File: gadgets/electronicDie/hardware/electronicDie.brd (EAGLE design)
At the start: 43.2 x 69.8 mm, 32 parts, among them IC1 CD4029N, IC2 NE555N, T1 BC327, T2 BC337, X1 USBPCB

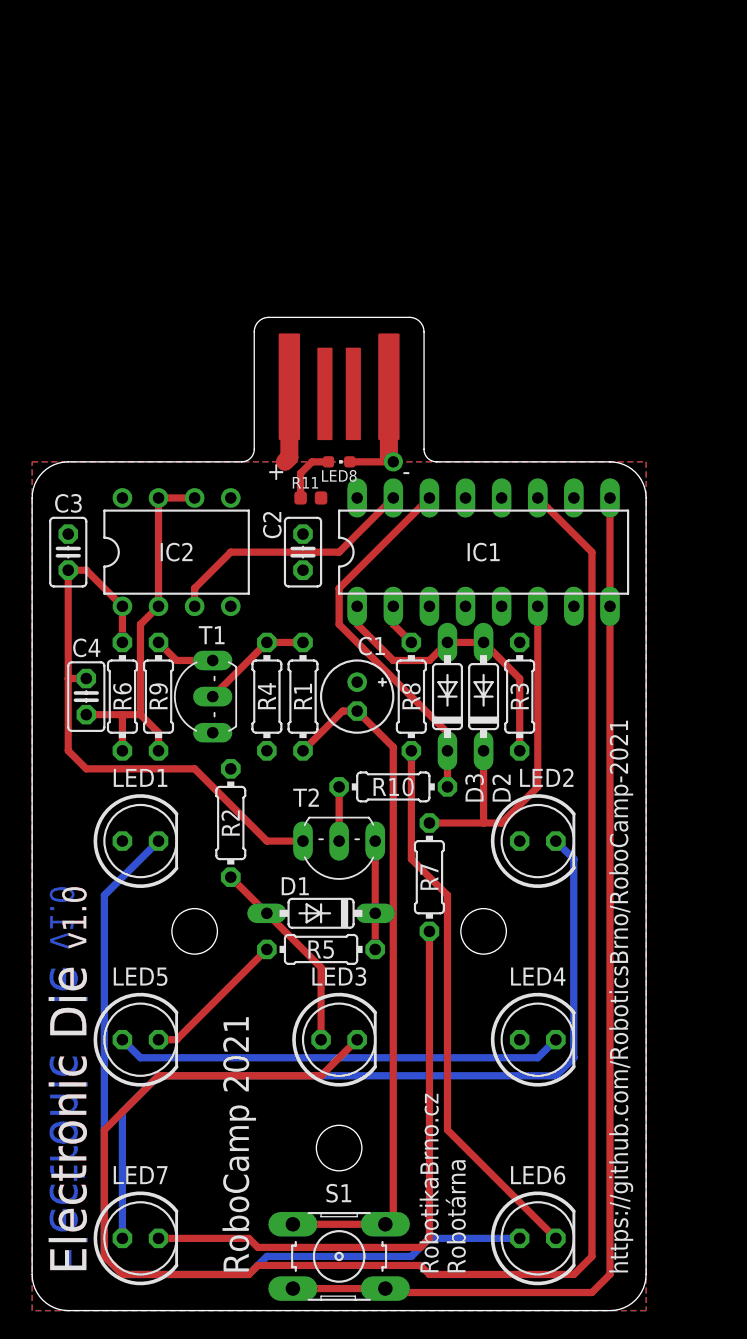
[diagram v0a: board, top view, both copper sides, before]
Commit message: ElectronicDie: fix v1.0 problems - make it bigger - change resistors and diodes package size - make larger spaces between parts - minimize part types - fix PNP transistor pinout - remove SMD power LED
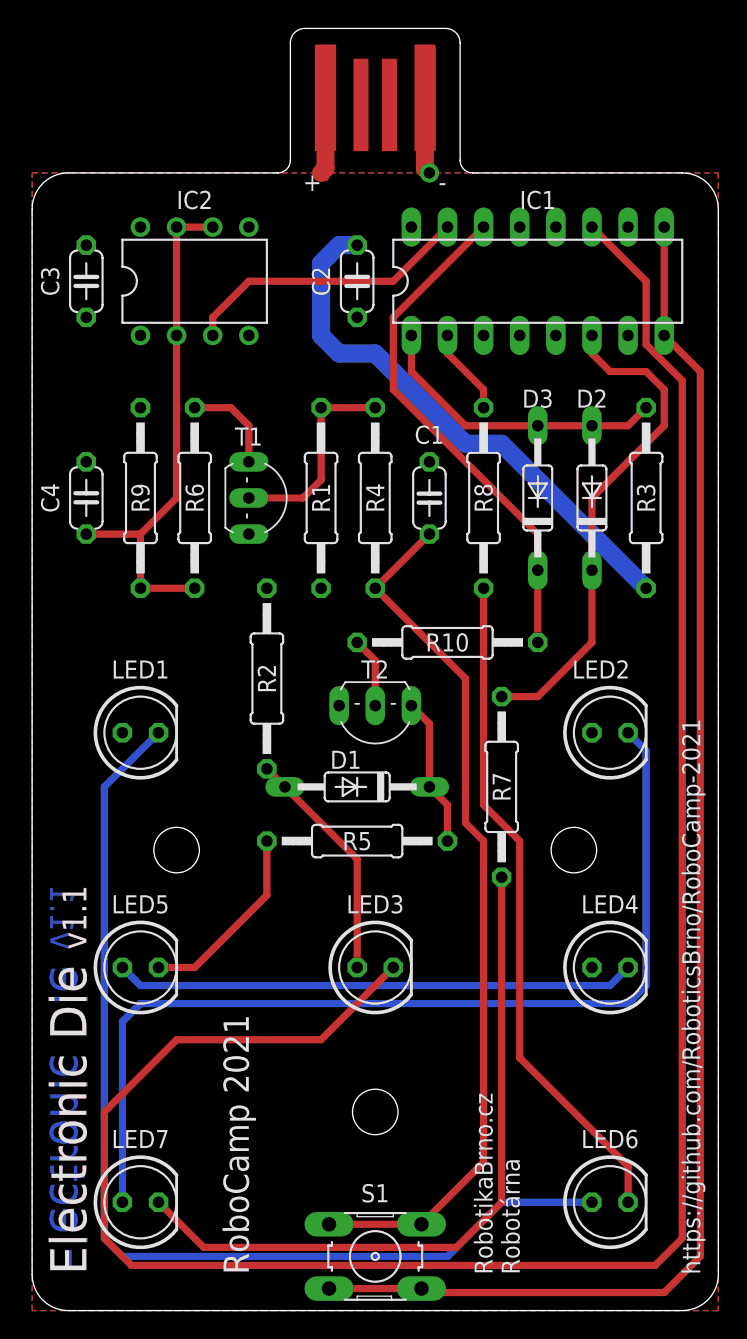
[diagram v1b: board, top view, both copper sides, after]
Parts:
- removed LED8: green, led:CHIPLED_0603
- removed R11: 1k, rcl_upravena:R0603
- C1: value 1u -> 100n; device rcl_upravena:E2-5 -> rcl_upravena:C050-024X044
- C2, C3, C4: device rcl_upravena:C025-025X050 -> rcl_upravena:C050-024X044
- D1, D2, D3: device diode:DO35-7 -> diode:DO35-10
- R1: value 3M3 -> 4M7; device rcl_upravena:0204/7 -> rcl_upravena:0207/12
- R10, R3: value 100k -> 10k; device rcl_upravena:0204/7 -> rcl_upravena:0207/12
- R2, R5, R6, R7, R8, R9: device rcl_upravena:0204/7 -> rcl_upravena:0207/12
- R4: value 10M -> 4M7; device rcl_upravena:0204/7 -> rcl_upravena:0207/12
- T1: value BC327 -> BC557B; device transistor:TO92-EBC -> transistor:TO92-CBE
- T2: value BC337 -> BC547B
- moved X1 20.5 mm to (24.1, 85.1)
- moved C2 19.4 mm to (22.9, 72.4)
- moved IC1 19.4 mm to (35.6, 72.4)
- moved C3 19.1 mm to (3.81, 72.4)
- moved IC2 19.1 mm to (11.4, 72.4)
- moved R3 16.6 mm to (43.2, 57.1), turned to 270 degrees
- moved D2 15.9 mm to (39.4, 57.1)
- moved D3 15.3 mm to (35.6, 57.1)
- moved C1 14.9 mm to (27.9, 57.1)
- moved R4 14.9 mm to (24.1, 57.1)
- moved R8 14.9 mm to (31.8, 57.1)
- moved R1 14.5 mm to (20.3, 57.1)
- moved T1 14.5 mm to (15.2, 57.1), turned to 270 degrees
- moved R6 14.2 mm to (11.4, 57.1)
- moved R9 14.0 mm to (7.62, 57.1)
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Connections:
- removed net N$3: LED8.A, R11.1
- net +5V: now also C1.1; no longer C1.+, R11.2
- net GND: no longer LED8.C
- net N$1: now also C1.2; no longer C1.-
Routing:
- net +5V: track 5.41 -> 44.4 mm
- net N$20: track 120.1 -> 149.4 mm
- net GND: track 126.5 -> 106.1 mm
- net N$1: track 48.8 -> 61.6 mm
- net N$16: track 61.6 -> 73.5 mm
- net N$14: track 58.0 -> 68.9 mm
- net N$11: track 26.1 -> 36.0 mm
- net N$5: track 27.7 -> 36.6 mm
- net N$22: track 38.5 -> 47.4 mm
- net N$10: track 26.5 -> 35.2 mm
- net N$8: track 41.2 -> 49.6 mm
- net N$2: track 7.93 -> 14.5 mm
- net N$13: track 31.5 -> 36.6 mm
- net N$3: track 4.03 -> 0.00 mm
- net N$18: track 10.3 -> 13.5 mm
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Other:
- board size 43.2 x 69.8 mm -> 48.3 x 90.2 mm
- board text added: "v1.1"
- board text removed: "v1.0"

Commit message: ElectronicDie v1.2: more resistant to assembly errors - resistors with same value grouped together - diodes grouped together - larger spaces between parts - 2k2 resistor replaced with 2 × 1k (so only 3 types of resistors left: 1k, 10k and 4M7) - added parts value to silkscreen - URL in silkscreen changed from robotikabrno.cz to robotickytabor.cz - changed year of Robocamp to 2022 (but 2021 remains in repo URL) - added silkscreen label for engraving owner name
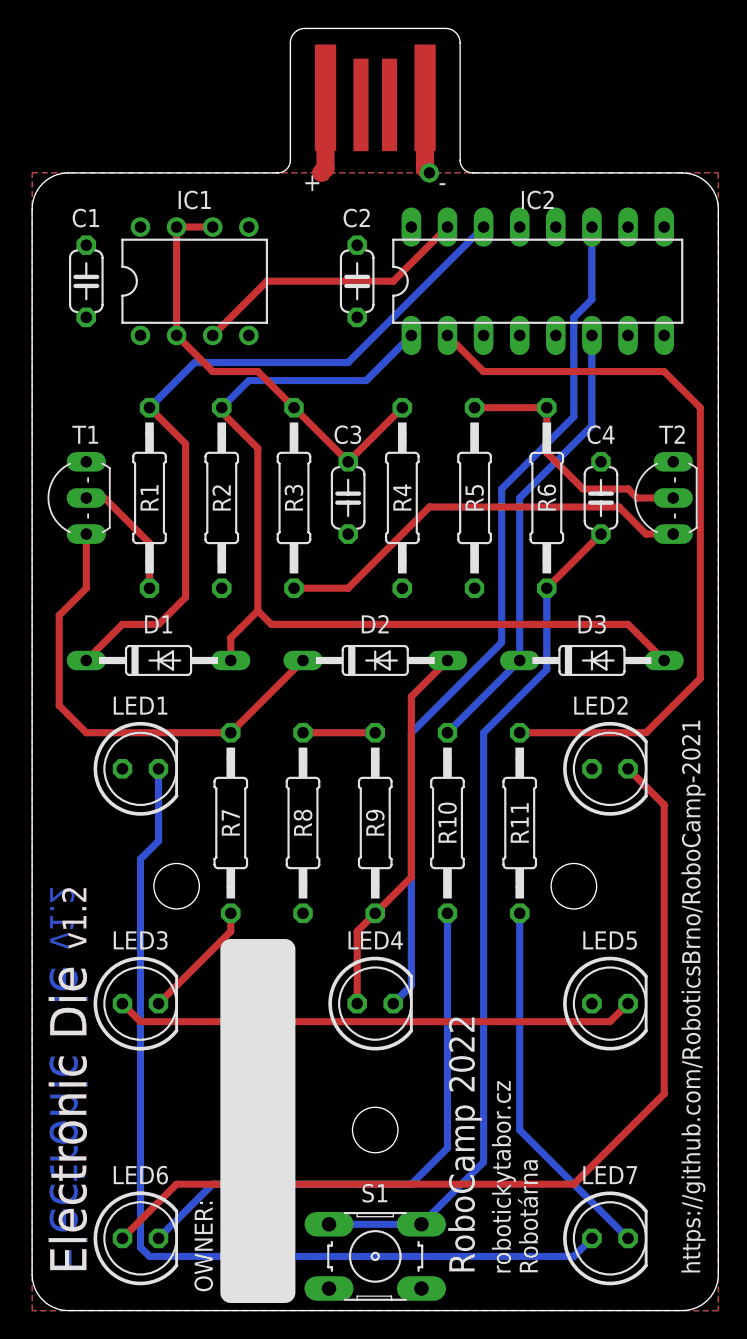
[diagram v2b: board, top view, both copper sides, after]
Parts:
- added R11: 1k, rcl_upravena:0207/12
- IC1: value CD4029N -> NE555N; device 40xx:DIL16 -> 555:DIL08
- IC2: value NE555N -> CD4029N; device 555:DIL08 -> 40xx:DIL16
- R1: value 4M7 -> 10k
- R10: value 10k -> 1k
- R2: value 2k2 -> 10k
- R5: value 1k -> 4M7
- R6: value 10k -> 4M7
- R9: value 4M7 -> 1k
- T1: value BC557B -> BC547B
- T2: value BC547B -> BC557B
- moved C4 36.2 mm to (40.0, 57.1), turned to 270 degrees
- moved LED5 33.1 mm to (40.6, 21.6)
- moved LED6 33.1 mm to (7.62, 5.08)
- moved LED7 33.1 mm to (40.6, 5.08)
- moved C1 28.5 mm to (3.81, 72.4)
- moved R9 28.2 mm to (24.1, 34.3), turned to 90 degrees
- moved R8 26.2 mm to (19.1, 34.3)
- moved T2 25.5 mm to (45.1, 57.1), turned to 90 degrees
- moved R5 25.5 mm to (31.1, 57.1), turned to 270 degrees
- moved R3 24.8 mm to (18.4, 57.1)
- moved R6 24.8 mm to (36.2, 57.1)
- moved IC1 24.1 mm to (11.4, 72.4)
- moved IC2 24.1 mm to (35.6, 72.4)
- moved C3 23.9 mm to (22.2, 57.1)
- moved R7 19.2 mm to (14.0, 34.3)
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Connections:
- new net N$3: R8.1, R9.2
- net +5V: now also C4.1, IC1.8, IC2.10, IC2.16, IC2.3, LED5.A, R5.2, R8.2, T2.E; no longer C3.1, IC1.10, IC1.16, IC1.3, IC2.8, LED4.A, R1.2, R3.2, T1.E
- net GND: now also C1.2, IC1.1, IC2.12, IC2.13, IC2.5, IC2.8, IC2.9, R4.1, T1.E; no longer C4.2, IC1.12, IC1.13, IC1.5, IC1.8, IC1.9, IC2.1, R9.1, T2.E
- net N$1: now also C4.2, R6.1; no longer C1.2, R4.1
- net N$10: now also D3.C, IC2.6, R10.1; no longer D2.C, IC1.6, R7.1
- net N$11: now also D1.C, IC2.14, R1.1; no longer D3.C, IC1.14, R10.1
- net N$12: now also IC2.2, R11.1; no longer IC1.2, R8.1
- net N$13: now also LED3.A, LED5.K; no longer LED4.K, LED5.A
- net N$14: now also LED6.A; no longer LED7.A
- net N$15: now also IC2.7; no longer IC1.7
- net N$16: now also LED7.A; no longer LED6.A
- net N$17: now also R1.2, T1.B; no longer R10.2, T2.B
- net N$18: now also LED3.K, R7.2; no longer LED5.K, R5.2
- net N$19: now also D2.A, LED4.A, R9.1; no longer D1.A, LED3.A, R2.1
- net N$2: now also R5.1, R6.2, T2.B; no longer R1.1, R4.2, T1.B
- net N$20: now also IC2.11, LED4.K; no longer IC1.11, LED3.K
- net N$21: now also D2.C, R7.1, T1.C; no longer D1.C, R5.1, T2.C
- net N$22: now also LED7.K, R11.2; no longer LED6.K, R8.2
- net N$4: now also R3.2, T2.C; no longer R6.2, T1.C
- net N$5: now also C3.1, IC1.2, IC1.6, IC1.7, R3.1, R4.2; no longer C4.1, IC2.2, IC2.6, IC2.7, R6.1, R9.2
- net N$6: now also IC1.5; no longer IC2.5
- net N$7: now also IC1.3, IC2.15; no longer IC1.15, IC2.3
- net N$8: now also LED6.K, R10.2; no longer LED7.K, R7.2
- net N$9: now also D1.A, IC2.1, R2.1; no longer D2.A, IC1.1, R3.1
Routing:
- net GND: track 106.1 -> 5.41 mm
- net N$20: track 149.4 -> 60.4 mm
- net N$12: track 6.13 -> 53.2 mm
- net N$9: track 21.2 -> 65.1 mm
- net +5V: track 44.4 -> 6.03 mm
- net N$4: track 6.88 -> 29.8 mm
- net N$21: track 10.6 -> 32.9 mm
- net N$22: track 47.4 -> 26.0 mm
- net N$11: track 36.0 -> 52.0 mm
- net N$8: track 49.6 -> 39.5 mm
- net N$19: track 16.6 -> 26.8 mm
- net N$16: track 73.5 -> 66.7 mm
- net N$5: track 36.6 -> 31.3 mm
- net N$18: track 13.5 -> 8.45 mm
- net N$3: track 0.00 -> 5.08 mm
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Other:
- board text added: "OWNER:"
- board text added: "RoboCamp 2022"
- board text added: "robotickytabor.cz Robotárna"
- board text added: "v1.2"
- board text removed: "RoboCamp 2021"
- board text removed: "RobotikaBrno.cz Robotárna"
- board text removed: "v1.1"
